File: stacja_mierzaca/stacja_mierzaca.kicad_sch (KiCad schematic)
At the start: 13 parts, among them M1 HW373-TP4056, Q1 PMOS, U1 ESP32-WROOM32-DEVKIT-V1-30P, U2 DS18B20, U3 Ai-Thinker-Ra-02

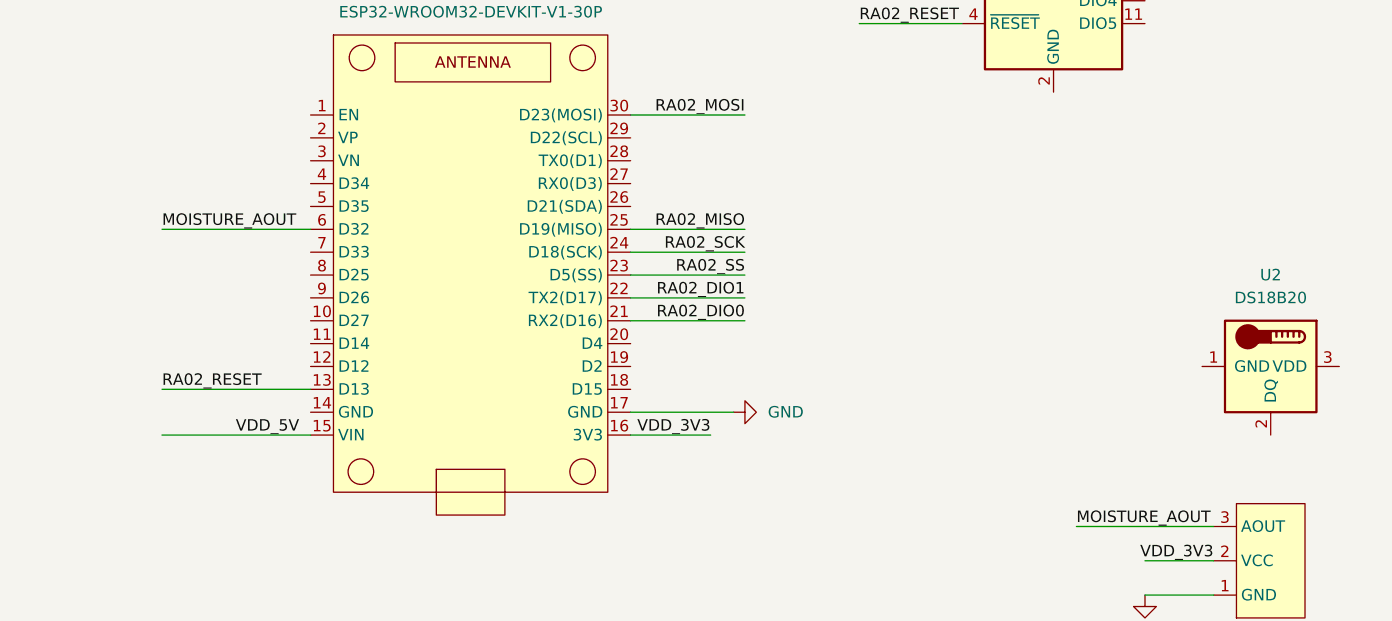
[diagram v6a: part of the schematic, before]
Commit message: feat(esp): add simple station transmitter
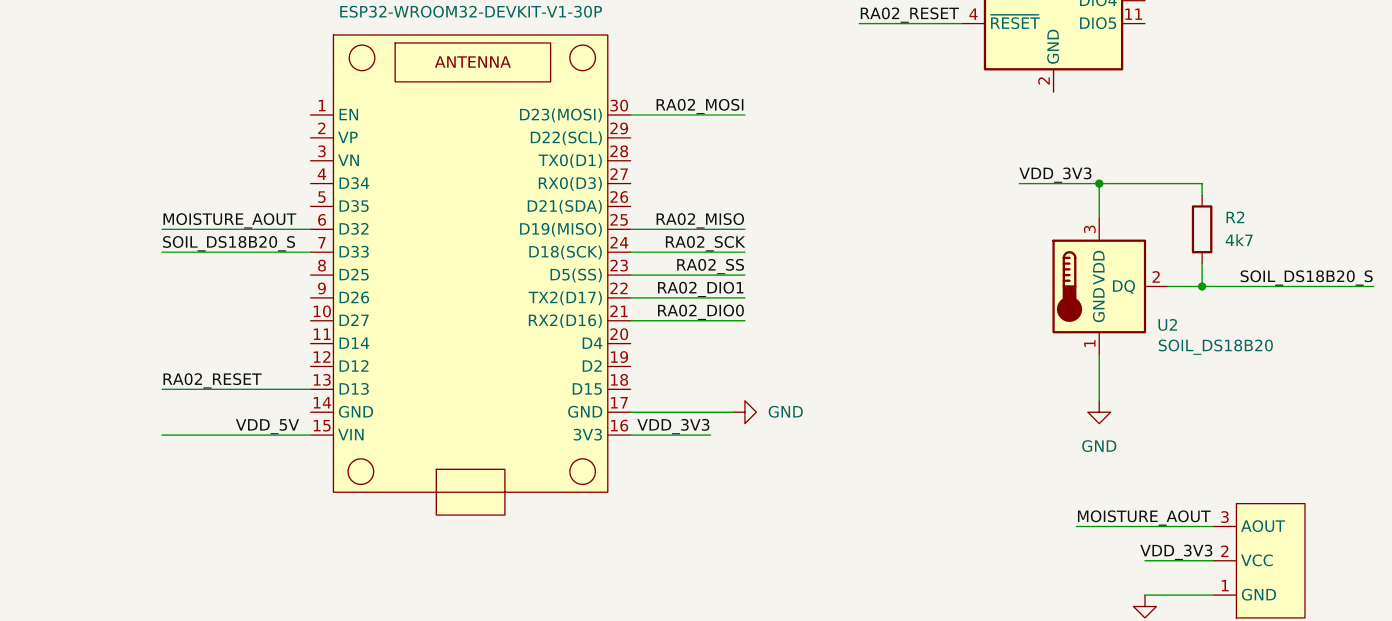
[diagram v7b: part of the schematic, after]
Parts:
- added R2: 4k7, symbol Device:R
- U2: value DS18B20 -> SOIL_DS18B20
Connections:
- net GND: now also U2.1 (GND)
- net VDD_3V3: now also U2.3 (VDD), R2.1
- net SOIL_DS18B20_S: now reaches U2.2 (DQ)
- net SOIL_DS18B20_S: now also U1.7 (D33), R2.2
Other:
- moved on the sheet: U2

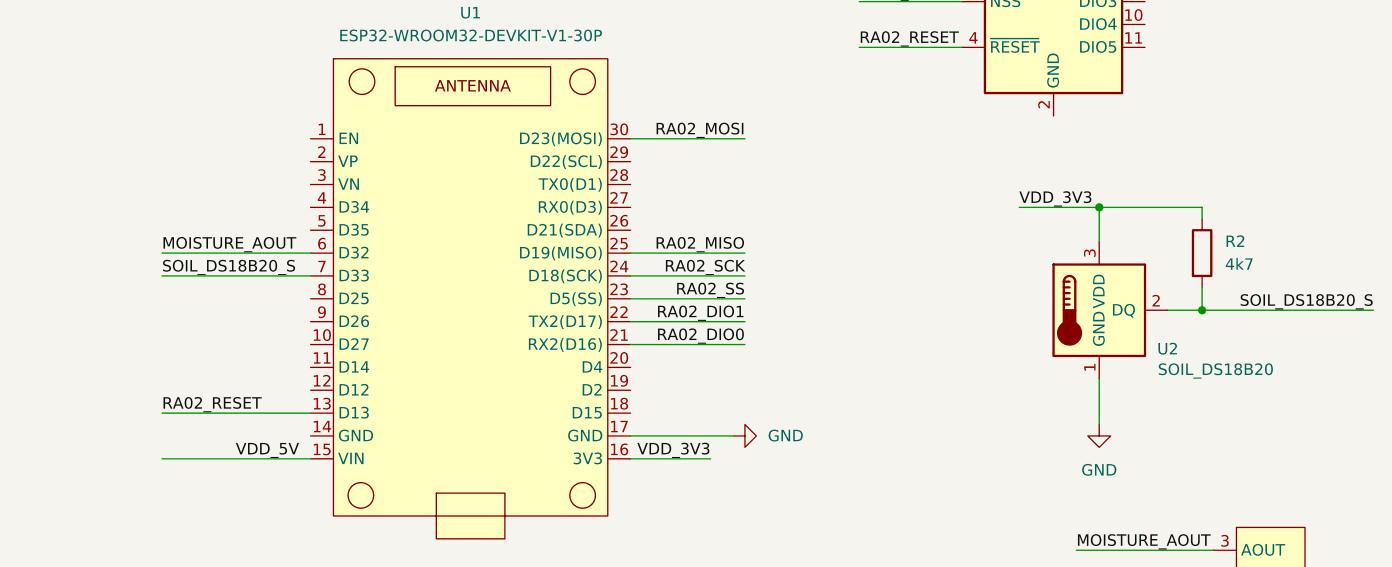
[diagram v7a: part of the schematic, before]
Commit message: feat(esp): add soil temp sensor
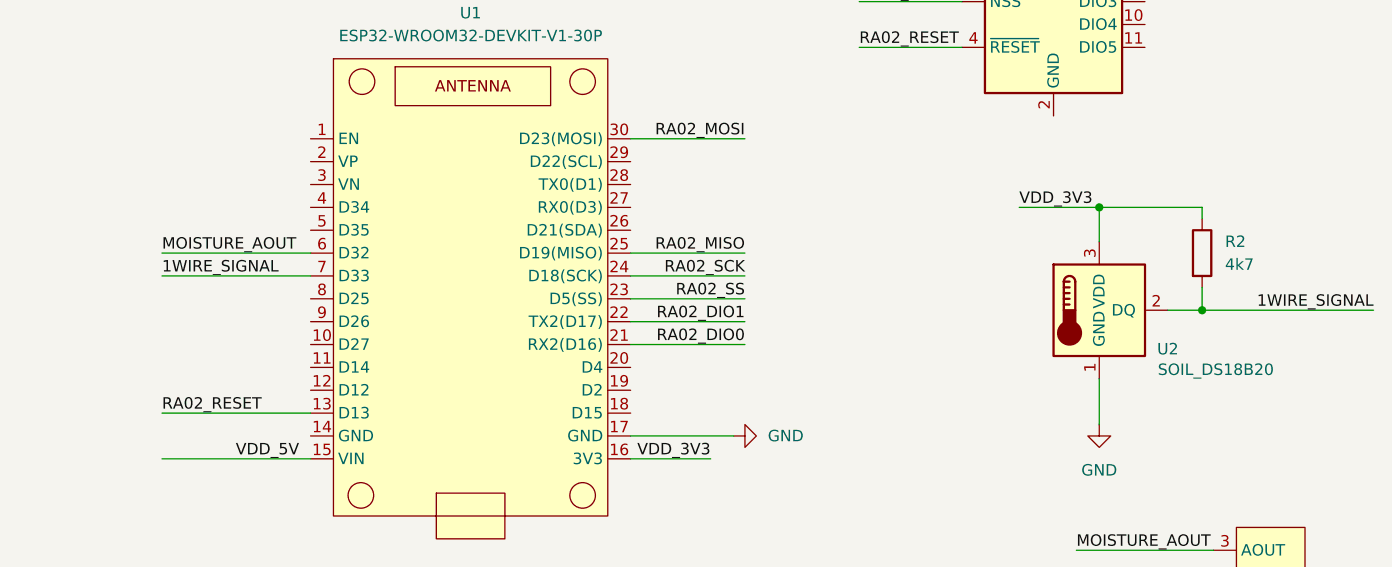
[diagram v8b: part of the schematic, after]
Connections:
- net SOIL_DS18B20_S renamed 1WIRE_SIGNAL
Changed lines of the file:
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@@
 		)
 	)
-	(label "SOIL_DS18B20_S"
+	(label "1WIRE_SIGNAL"
 		(at 138.43 109.22 0)
 		(effects
@@
 		)
 	)
-	(label "SOIL_DS18B20_S"
+	(label "1WIRE_SIGNAL"
 		(at 273.05 113.03 180)
 		(effects
